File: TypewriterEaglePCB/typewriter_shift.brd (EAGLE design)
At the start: 100 x 80 mm, 39 parts, among them IC2 MDC3105LT1, U0 TPIC6A595DW, U1 TPIC6A595DW, U2 TPIC6A595DW, U3 TPIC6A595DW, U4 TPIC6A595DW, U5 TPIC6A595DW, X1 5V power

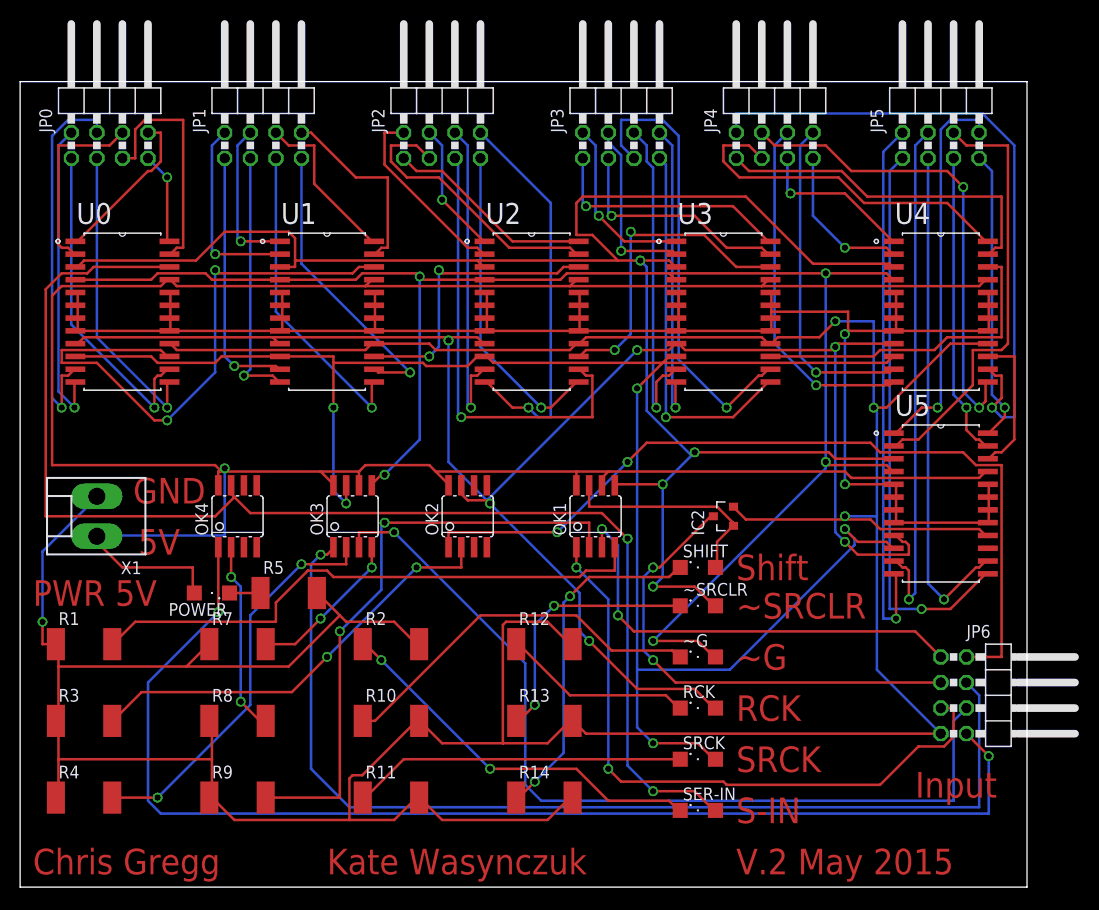
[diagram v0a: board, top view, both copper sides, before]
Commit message: latest update with resistors and LEDs
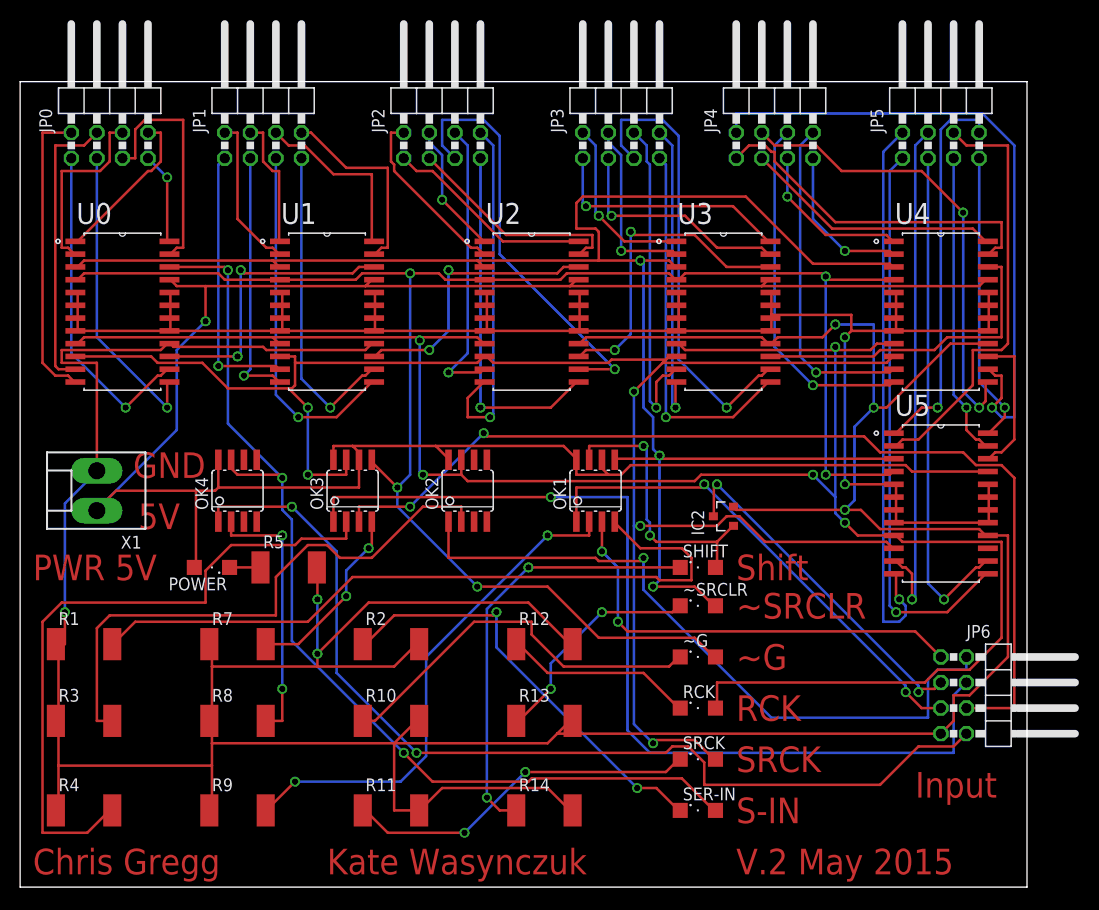
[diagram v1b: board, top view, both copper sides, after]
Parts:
- moved OK1 2.54 mm to (57.1, 39.4)
- moved OK2 2.54 mm to (44.5, 39.4)
- moved OK3 2.54 mm to (33.0, 39.4)
- moved OK4 2.54 mm to (21.6, 39.4)
- moved POWER 2.54 mm to (19.1, 31.8)
- moved R5 2.54 mm to (26.7, 31.8)
- moved X1 2.54 mm to (7.62, 39.4)
- moved R11 1.27 mm to (36.8, 7.62)
- moved R14 1.27 mm to (52.1, 7.62)
- moved R4 1.27 mm to (6.35, 7.62)
- moved R9 1.27 mm to (21.6, 7.62)
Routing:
- net N$7: track 130.5 -> 101.0 mm, vias 2 -> 3
- net N$1: track 58.2 -> 29.1 mm
- net N$76: track 39.7 -> 65.9 mm, vias 2 -> 0
- net VCC: track 252.5 -> 226.7 mm
- net N$70: track 174.4 -> 198.8 mm, vias 6 -> 5
- net N$30: track 121.0 -> 98.2 mm
- net N$11: track 64.4 -> 49.3 mm
- net N$78: track 56.9 -> 71.8 mm
- net N$23: track 83.6 -> 69.2 mm, vias 2 -> 1
- net N$77: track 43.0 -> 56.7 mm, vias 2 -> 0
- net N$15: track 47.6 -> 35.1 mm
- net N$68: track 164.4 -> 175.2 mm
- net N$31: track 88.4 -> 99.1 mm, vias 1 -> 2
- net N$18: track 38.6 -> 28.7 mm, vias 1 -> 0
- net N$53: track 35.5 -> 25.9 mm
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
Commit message: Updated circuit with correct resistances for optoisolators and LEDs
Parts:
- R1, R3, R4, R7, R8, R9: value 576 -> 200
- R10, R11, R12, R13, R14, R2: value 576 -> 150
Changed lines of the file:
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@@
 <attribute name="OC_FARNELL" value="1469512" x="1.27" y="58.42" size="1.778" layer="27" display="off"/>
 </element>
-<element name="R1" library="resistor" package="R2512" value="576" x="6.35" y="24.13"/>
-<element name="R3" library="resistor" package="R2512" value="576" x="6.35" y="16.51"/>
-<element name="R4" library="resistor" package="R2512" value="576" x="6.35" y="7.62"/>
-<element name="R7" library="resistor" package="R2512" value="576" x="21.59" y="24.13"/>
-<element name="R8" library="resistor" package="R2512" value="576" x="21.59" y="16.51"/>
-<element name="R9" library="resistor" package="R2512" value="576" x="21.59" y="7.62"/>
-<element name="R2" library="resistor" package="R2512" value="576" x="36.83" y="24.13"/>
-<element name="R10" library="resistor" package="R2512" value="576" x="36.83" y="16.51"/>
-<element name="R11" library="resistor" package="R2512" value="576" x="36.83" y="7.62"/>
-<element name="R12" library="resistor" package="R2512" value="576" x="52.07" y="24.13"/>
-<element name="R13" library="resistor" package="R2512" value="576" x="52.07" y="16.51"/>
-<element name="R14" library="resistor" package="R2512" value="576" x="52.07" y="7.62"/>
+<element name="R1" library="resistor" package="R2512" value="200" x="6.35" y="24.13"/>
+<element name="R3" library="resistor" package="R2512" value="200" x="6.35" y="16.51"/>
+<element name="R4" library="resistor" package="R2512" value="200" x="6.35" y="7.62"/>
+<element name="R7" library="resistor" package="R2512" value="200" x="21.59" y="24.13"/>
+<element name="R8" library="resistor" package="R2512" value="200" x="21.59" y="16.51"/>
+<element name="R9" library="resistor" package="R2512" value="200" x="21.59" y="7.62"/>
+<element name="R2" library="resistor" package="R2512" value="150" x="36.83" y="24.13"/>
+<element name="R10" library="resistor" package="R2512" value="150" x="36.83" y="16.51"/>
+<element name="R11" library="resistor" package="R2512" value="150" x="36.83" y="7.62"/>
+<element name="R12" library="resistor" package="R2512" value="150" x="52.07" y="24.13"/>
+<element name="R13" library="resistor" package="R2512" value="150" x="52.07" y="16.51"/>
+<element name="R14" library="resistor" package="R2512" value="150" x="52.07" y="7.62"/>
 <element name="RCK" library="led" package="SML1206" value="rck" x="67.31" y="17.78"/>
 <element name="~SRCLR" library="led" package="SML1206" value="~srclr" x="67.31" y="27.94"/>

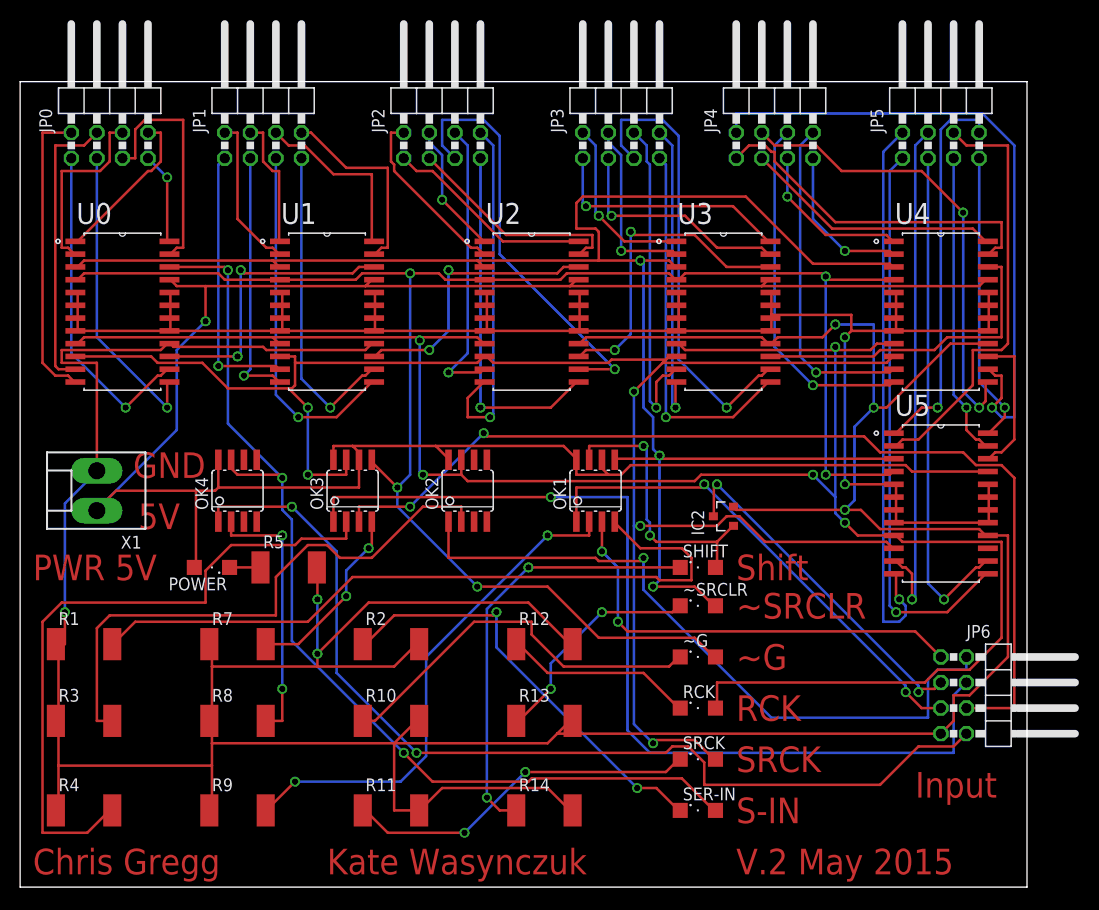
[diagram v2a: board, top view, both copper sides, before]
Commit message: Added wide power ground traces and 1206 resistors
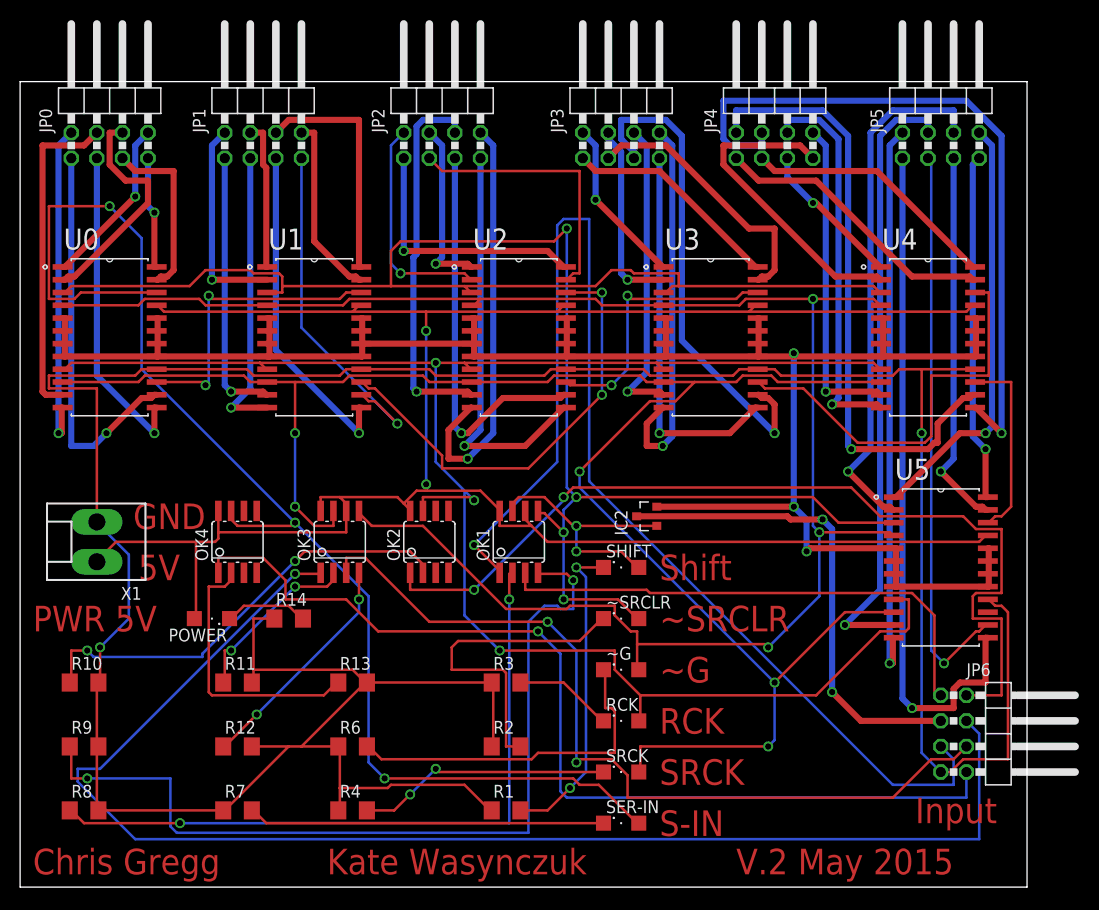
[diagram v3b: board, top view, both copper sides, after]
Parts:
- removed R5: 576, resistor:R2512
- added R6: 150, resistor:R1206
- R1, R3, R4, R7: value 200 -> 150; device resistor:R2512 -> resistor:R1206
- R10, R11, R12, R13, R14: value 150 -> 200; device resistor:R2512 -> resistor:R1206
- R2, R8, R9: device resistor:R2512 -> resistor:R1206
- moved R1 45.0 mm to (48.3, 7.62)
- moved R3 42.1 mm to (48.3, 20.3)
- moved R12 32.1 mm to (21.6, 14.0)
- moved R14 31.8 mm to (26.7, 26.7)
- moved R10 30.7 mm to (6.35, 20.3)
- moved R4 26.7 mm to (33.0, 7.62)
- moved R11 19.8 mm to (21.6, 20.3)
- moved R13 19.4 mm to (33.0, 20.3)
- moved R8 17.6 mm to (6.35, 7.62)
- moved R7 16.5 mm to (21.6, 7.62)
- moved R9 16.5 mm to (6.35, 14.0)
- moved R2 15.3 mm to (48.3, 14.0)
- moved OK1 9.16 mm to (49.5, 34.3)
- moved RCK 7.73 mm to (59.7, 16.5)
- moved SER-IN 7.73 mm to (59.7, 6.35)
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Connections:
- net GND: now also R14.1, R2.1, R6.1, R8.2, R9.2; no longer IC2.2, R14.2, R2.2, R5.2, R8.1, R9.1
- net GNDA: now also IC2.2
- net N$17: now also R8.1; no longer R9.2
- net N$32: now also R12.1; no longer R7.2
- net N$6: now also R3.2; no longer R12.1
- net N$72: now also R13.1; no longer R8.2
- net N$73: now also R1.2; no longer R14.1
- net N$74: now also R4.2; no longer R11.1
- net N$75: now also R6.2; no longer R10.1
- net N$76: now also R11.1; no longer R4.2
- net N$77: now also R10.1; no longer R3.2
- net N$78: now also R9.1; no longer R1.2
- net N$79: now also R7.2; no longer R2.1
- net N$8: now also R2.2; no longer R13.1
- net N$80: now also R14.2; no longer R5.1
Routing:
- net GND: track 397.3 -> 312.0 mm, vias 6 -> 2
- net N$11: track 49.3 -> 121.5 mm, vias 2 -> 1
- net N$76: track 65.9 -> 17.8 mm, vias 0 -> 2
- net N$29: track 95.6 -> 137.7 mm
- net N$7: track 101.0 -> 129.0 mm
- net N$58: track 46.3 -> 71.4 mm, vias 2 -> 1
- net N$23: track 69.2 -> 92.1 mm, vias 1 -> 2
- net N$70: track 198.8 -> 177.3 mm, vias 5 -> 3
- net N$71: track 173.3 -> 194.6 mm, vias 3 -> 4
- net GNDA: track 173.5 -> 194.5 mm, vias 2 -> 3
- net N$17: track 50.6 -> 69.4 mm
- net N$2: track 27.8 -> 45.0 mm
- net N$55: track 15.5 -> 31.7 mm, vias 1 -> 0
- net N$31: track 99.1 -> 83.1 mm
- net N$78: track 71.8 -> 86.7 mm, vias 0 -> 2
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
